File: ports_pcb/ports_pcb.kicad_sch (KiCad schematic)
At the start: 58 parts, among them J1 Conn_01x01_Socket, J10 Conn_01x01_Socket, J100 Joystick, J101 RGB, J102 Printer, J103 Video, J104 Junet, J105 Junet, J106 Tape, J107 5V/2A, J11 Conn_01x01_Socket, J12 Conn_01x01_Socket, J13 Conn_01x01_Socket, J14 Conn_01x01_Socket, J15 Conn_01x01_Socket, J16 Conn_01x01_Socket, J17 Conn_01x01_Socket, J18 Conn_01x01_Socket, J19 Conn_01x01_Socket, J2 Conn_01x01_Socket, J20 Conn_01x01_Socket, J21 Conn_01x01_Socket, J22 Conn_01x01_Socket, J23 Conn_01x01_Socket, J24 Conn_01x01_Socket, J3 Conn_01x01_Socket, J30 Conn_01x01_Socket, J31 Conn_01x01_Socket, J32 Conn_01x01_Socket, J33 Conn_01x01_Socket, J34 Conn_01x01_Socket, J35 Conn_01x01_Socket, J36 Conn_01x01_Socket, J4 Conn_01x01_Socket, J41 RESET1, J42 RESET2, J43 Conn_01x01_Socket, J44 Conn_01x01_Socket, J45 Conn_01x01_Socket, J46 Conn_01x01_Socket, J47 Conn_01x01_Socket, J48 Conn_01x01_Socket, J49 Conn_01x01_Socket, J5 Conn_01x01_Socket, J50 Conn_01x01_Socket, J51 Conn_01x01_Socket, J52 Conn_01x01_Socket, J53 Conn_01x01_Socket, J6 Conn_01x01_Socket, J7 Conn_01x01_Socket, J8 Conn_01x01_Socket, J9 Conn_01x01_Socket, SW1 Reset, SW2 Power

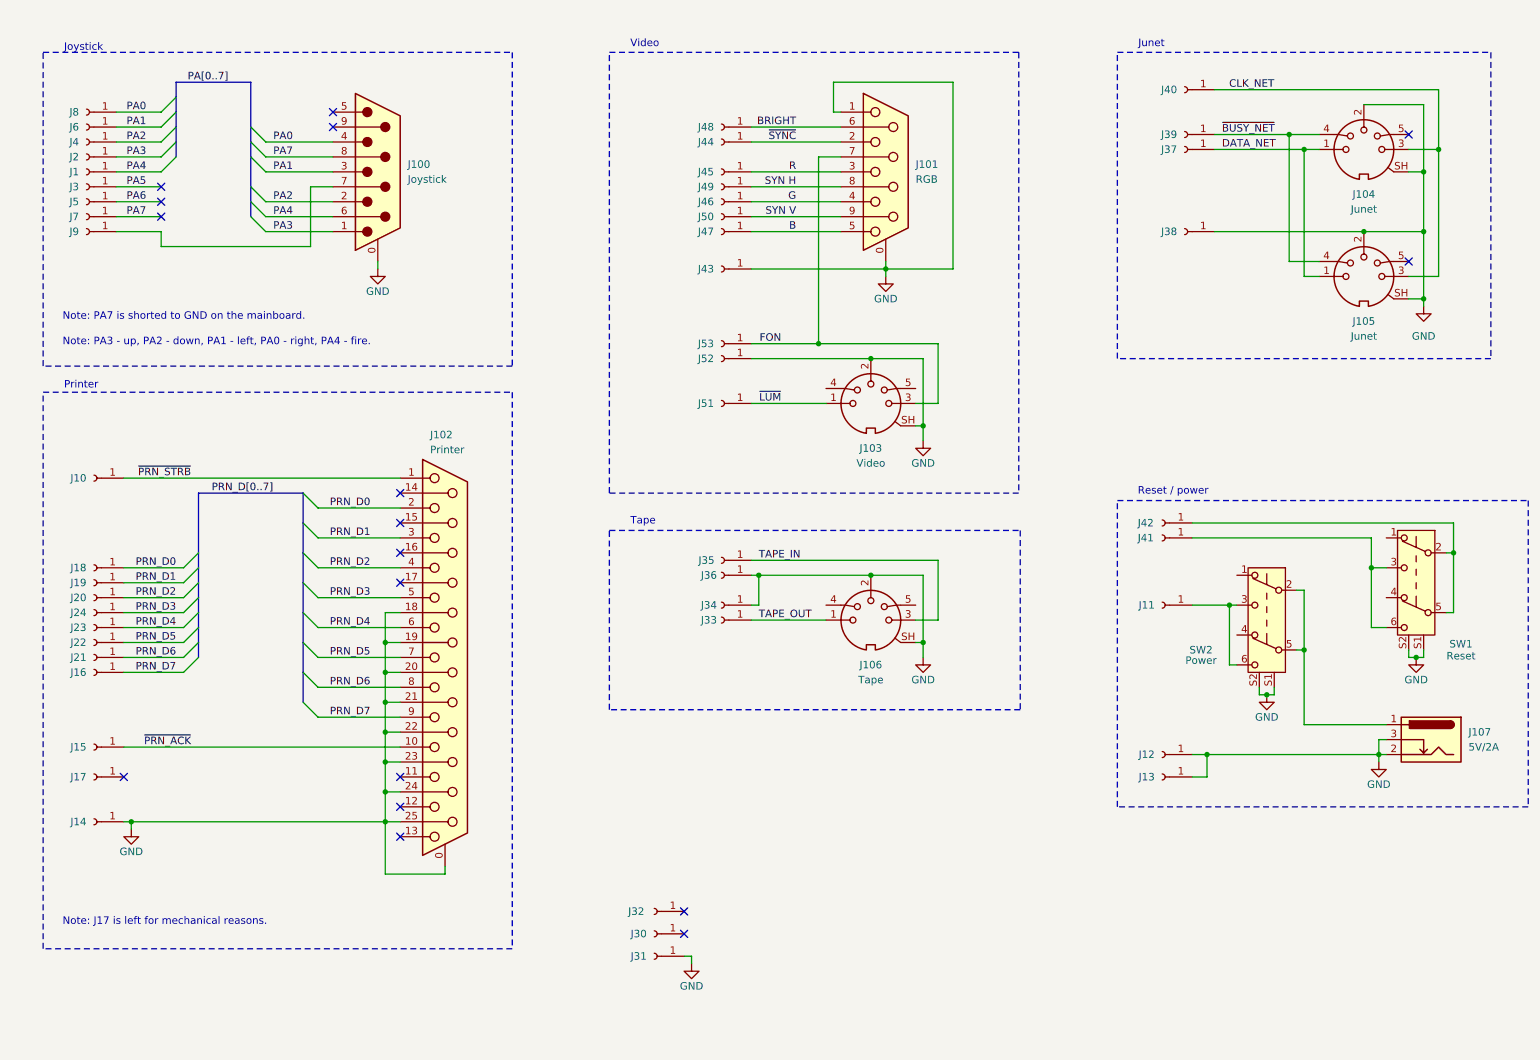
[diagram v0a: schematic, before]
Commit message: ports_pcb: converted to KiCAD 9, fixed 3d models (#1)
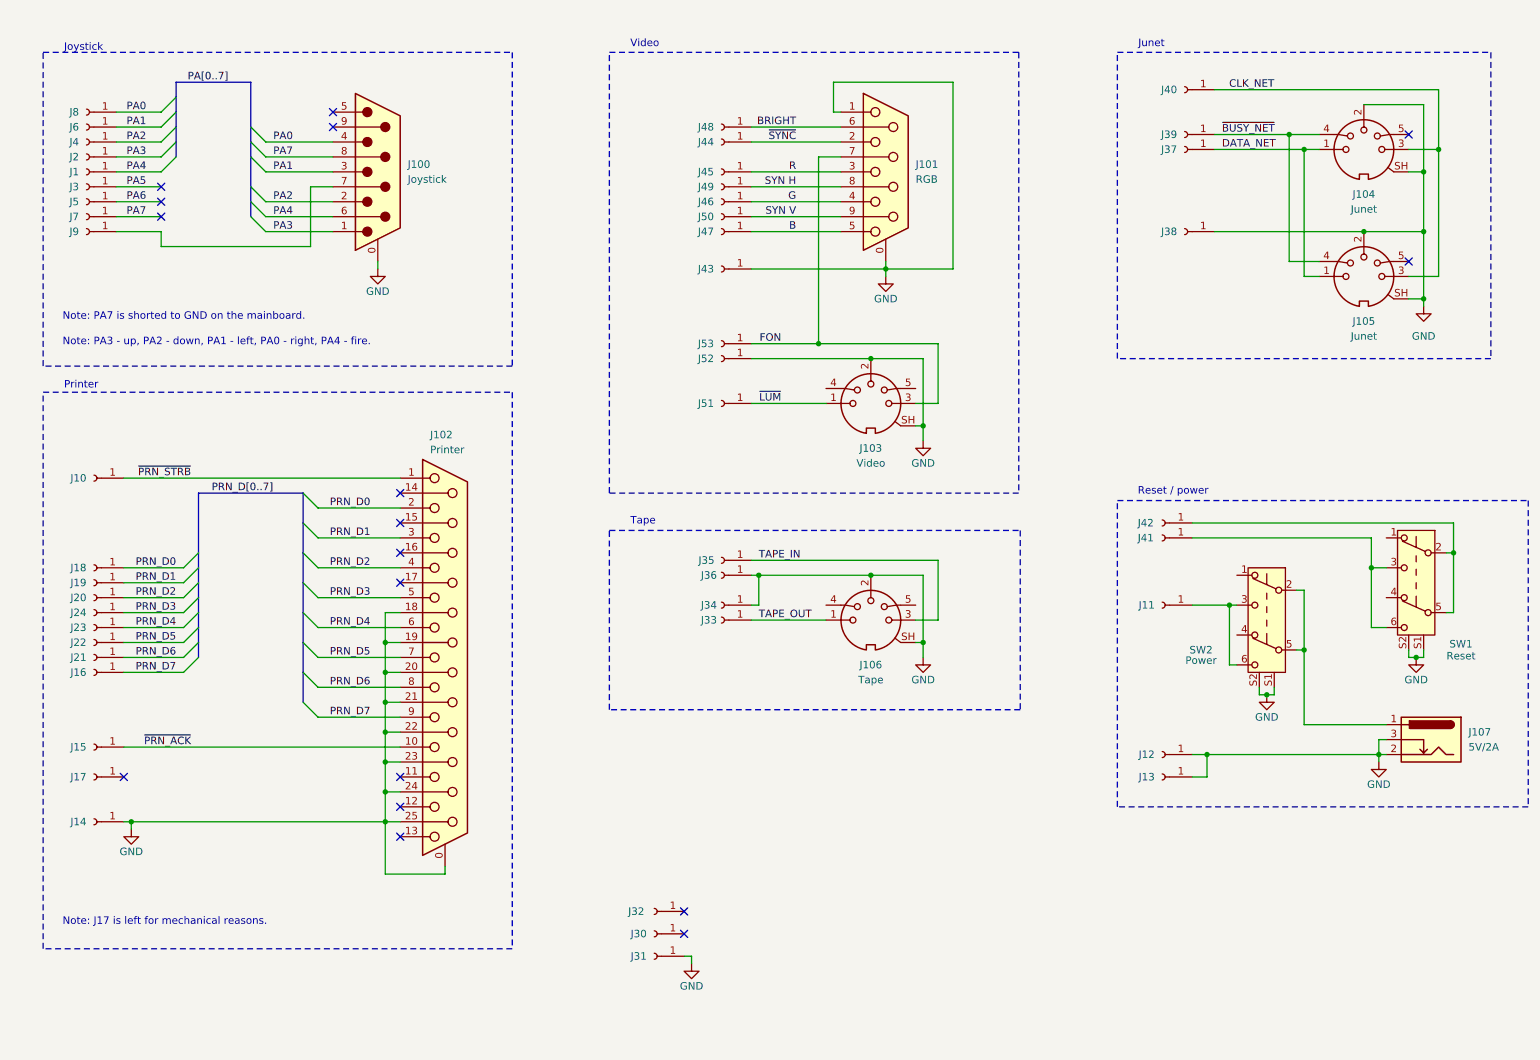
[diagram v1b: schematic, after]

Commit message: Ports PCB: reworked joy (#8) and video (#10)
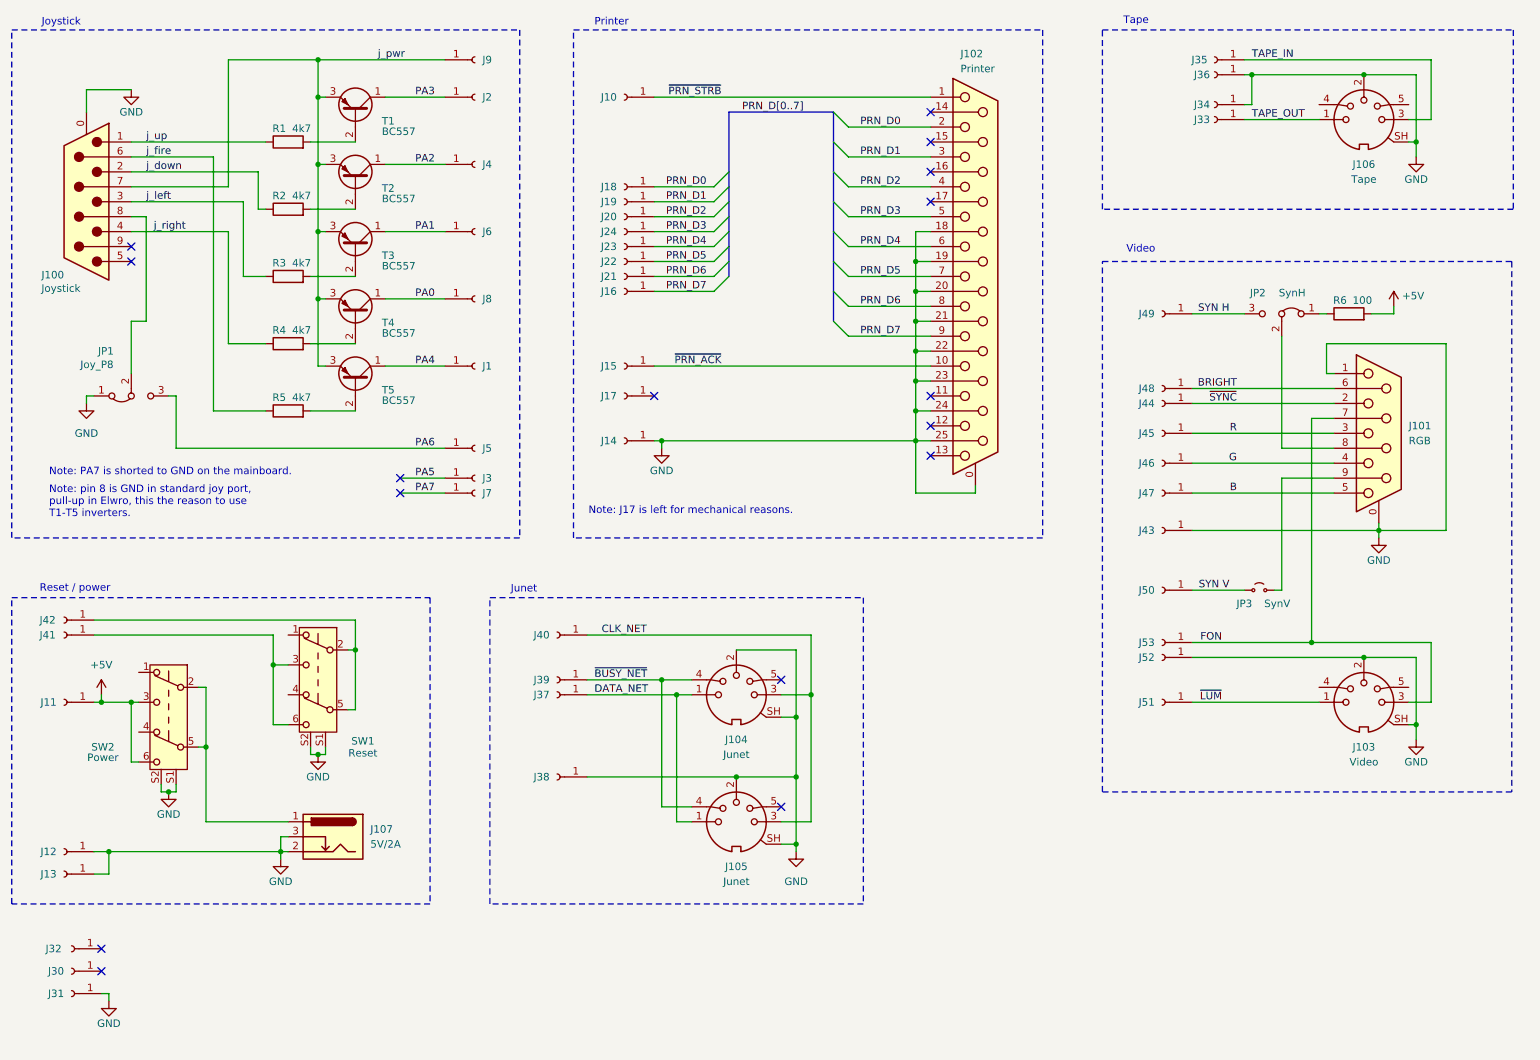
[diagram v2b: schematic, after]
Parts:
- added JP1: Joy_P8, Connector_PinHeader_2.54mm:PinHeader_1x03_P2.54mm_Vertical, symbol Jumper:Jumper_3_Bridged12
- added JP2: SynH, Connector_PinHeader_2.54mm:PinHeader_1x03_P2.54mm_Vertical, symbol Jumper:Jumper_3_Bridged12
- added JP3: SynV, Connector_PinHeader_2.54mm:PinHeader_1x02_P2.54mm_Vertical, symbol Jumper:Jumper_2_Small_Open
- added R1, R2, R3, R4, R5: 4k7, Resistor_THT:R_Axial_DIN0207_L6.3mm_D2.5mm_P10.16mm_Horizontal, symbol Device:R
- added R6: 100, Resistor_THT:R_Axial_DIN0207_L6.3mm_D2.5mm_P10.16mm_Horizontal, symbol Device:R
- added T1, T2, T3, T4, T5: BC557, Package_TO_SOT_THT:TO-92_Inline, symbol Transistor_BJT:BC557
- J100: footprint Connector_Dsub:DSUB-9_Male_Horizontal_P2.77x2.84mm_EdgePinOffset7.70mm_Housed_MountingHolesOffset9.12mm -> Connector_Dsub:DSUB-9_Pins_Horizontal_P2.77x2.84mm_EdgePinOffset7.70mm_Housed_MountingHolesOffset9.12mm
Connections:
- net GND: now also JP1.1 (A)
- net PA0: now also T4.1 (C); no longer J100.4
- net PA1: now also T3.1 (C); no longer J100.3
- net PA2: now also T2.1 (C); no longer J100.2
- net PA3: now also T1.1 (C); no longer J100.1
- net PA4: now also T5.1 (C); no longer J100.6
- net PA6: now also JP1.3 (B)
- net PA7: no longer J100.8
- net SYN H: now also JP2.3 (B); no longer J101.8
- net SYN V: now also JP3.2 (B); no longer J101.9
- net j_pwr: now reaches J100.7, J9.1 (Pin_1)
- net j_pwr: now also T1.3 (E), T2.3 (E), T3.3 (E), T4.3 (E), T5.3 (E)
- net +5V: now reaches J11.1 (Pin_1), SW2.3 (C), SW2.6 (C)
- net +5V: now also R6.2
- new net: JP2.1 (A), R6.1
- new net: R2.2, T2.2 (B)
- new net: R4.2, T4.2 (B)
- new net: J101.8, JP2.2 (C)
- new net: J101.9, JP3.1 (A)
- new net: R3.2, T3.2 (B)
- new net: J100.8, JP1.2 (C)
- new net: R1.2, T1.2 (B)
- new net: R5.2, T5.2 (B)
- new net j_down: J100.2, R2.1
- new net j_fire: J100.6, R5.1
- new net j_left: J100.3, R3.1
- new net j_right: J100.4, R4.1
- new net j_up: J100.1, R1.1
- no-connect marks 17 -> 16
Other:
- note added: "Note: pin 8 is GND in standard joy port, pull-up in Elwro, this the reason to use T1-T5 inverters."
- note removed: "Note: PA3 - up, PA2 - down, PA1 - left, PA0 - right, PA4 - fire."
- moved on the sheet: J1, J10, J101, J102, J103, J104, J105, J106, J107, J11, J12, J13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

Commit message: ports_pcb: added fuse, aux power connector, changed DIN 3d model
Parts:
- added C1: 100nF, Capacitor_THT:C_Disc_D5.0mm_W2.5mm_P2.50mm, symbol Device:C_Small
- added F1: 2A, Fuse:Fuseholder_Clip-5x20mm_Littelfuse_445-030_Inline_P20.50x5.20mm_D1.30mm_Horizontal, symbol Device:Fuse
- added J108: Conn_01x02, Connector_Molex:Molex_KK-254_AE-6410-02A_1x02_P2.54mm_Vertical, symbol Connector_Generic:Conn_01x02
- J101: footprint Connector_Dsub:DSUB-9_Female_Horizontal_P2.77x2.84mm_EdgePinOffset7.70mm_Housed_MountingHolesOffset9.12mm -> Connector_Dsub:DSUB-9_Socket_Horizontal_P2.77x2.84mm_EdgePinOffset7.70mm_Housed_MountingHolesOffset9.12mm
- J102: footprint Connector_Dsub:DSUB-25_Female_Horizontal_P2.77x2.84mm_EdgePinOffset7.70mm_Housed_MountingHolesOffset9.12mm -> Connector_Dsub:DSUB-25_Socket_Horizontal_P2.77x2.84mm_EdgePinOffset7.70mm_Housed_MountingHolesOffset9.12mm
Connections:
- net +5V: now also J108.1 (Pin_1)
- net GND: now also C1.2, J108.2 (Pin_2)
- net at JP2.1 (A), R6.1: now also C1.1
- net at SW2.2 (B), SW2.5 (B): now also F1.1; no longer J107.1
- new net: F1.2, J107.1
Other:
- note added: "Note: pin 8 is GND in a standard joystick port, pull-up in Elwro, this is the reason for using T1-T5 inverters."
- note removed: "Note: pin 8 is GND in standard joy port, pull-up in Elwro, this the reason to use T1-T5 inverters."
- company: (none) -> Przemysław Węgrzyn <pwegrzyn@codepainters.com>
- title: (none) -> Elwro 800 Junio ports breakout board
- moved on the sheet: J101, J103, J43, J44, J45, J46, J47, J48, J49, J50, J51, J52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

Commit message: ports_pcb: fixed a typo in schematic title
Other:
- title: Elwro 800 Junio ports breakout board -> Elwro 800 Junior ports breakout board
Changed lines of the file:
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@@
 	(paper "A4")
 	(title_block
-		(title "Elwro 800 Junio ports breakout board")
+		(title "Elwro 800 Junior ports breakout board")
 		(rev "1.1")
 		(company "Przemysław Węgrzyn <pwegrzyn@codepainters.com>")

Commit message: ports_pcb: excluded Jx headers from BOM
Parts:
- J1, J10, J11, J12, J13, J14, J15, J16, J17, J18, J19, J2, J20, J21, J22, J23, J24, J3, J30, J31, J32, J33, J34, J35, J36, J37, J38, J39, J4, J40, J41, J42, J43, J44, J45, J46, J47, J48, J49, J5, J50, J51, J52, J53, J6, J7, J8, J9: now left out of the parts list
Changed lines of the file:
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@@
 		(unit 1)
 		(exclude_from_sim no)
-		(in_bom yes)
+		(in_bom no)
 		(on_board yes)
 		(dnp no)
@@
 		(unit 1)
 		(exclude_from_sim no)
-		(in_bom yes)
+		(in_bom no)
 		(on_board yes)
 		(dnp no)
@@
 		(unit 1)
 		(exclude_from_sim no)
-		(in_bom yes)
+		(in_bom no)
 		(on_board yes)
 		(dnp no)
@@
 		(unit 1)
 		(exclude_from_sim no)
-		(in_bom yes)
+		(in_bom no)
 		(on_board yes)
 		(dnp no)
@@
 		(unit 1)
 		(exclude_from_sim no)
-		(in_bom yes)
+		(in_bom no)
 		(on_board yes)
 		(dnp no)
@@
 		(unit 1)
 		(exclude_from_sim no)
-		(in_bom yes)
+		(in_bom no)
 		(on_board yes)
 		(dnp no)
@@
 		(unit 1)
 		(exclude_from_sim no)
-		(in_bom yes)
+		(in_bom no)
 		(on_board yes)
 		(dnp no)
@@
 		(unit 1)
 		(exclude_from_sim no)
-		(in_bom yes)
+		(in_bom no)
 		(on_board yes)
 		(dnp no)
@@
 		(unit 1)
 		(exclude_from_sim no)
-		(in_bom yes)
+		(in_bom no)
 		(on_board yes)
 		(dnp no)
@@
 		(unit 1)
 		(exclude_from_sim no)
-		(in_bom yes)
+		(in_bom no)
 		(on_board yes)
 		(dnp no)
@@
 		(unit 1)
 		(exclude_from_sim no)
-		(in_bom yes)
+		(in_bom no)
 		(on_board yes)
 		(dnp no)
@@
 		(unit 1)
 		(exclude_from_sim no)
-		(in_bom yes)
+		(in_bom no)
 		(on_board yes)
 		(dnp no)
@@
 		(unit 1)
 		(exclude_from_sim no)
-		(in_bom yes)
+		(in_bom no)
 		(on_board yes)
 		(dnp no)
@@
 		(unit 1)
 		(exclude_from_sim no)
-		(in_bom yes)
+		(in_bom no)
 		(on_board yes)
 		(dnp no)
@@
 		(unit 1)
 		(exclude_from_sim no)
-		(in_bom yes)
+		(in_bom no)
 		(on_board yes)
 		(dnp no)
@@
 		(unit 1)
 		(exclude_from_sim no)
-		(in_bom yes)
+		(in_bom no)
 		(on_board yes)
 		(dnp no)
@@
 		(unit 1)
 		(exclude_from_sim no)
-		(in_bom yes)
+		(in_bom no)
 		(on_board yes)
 		(dnp no)
@@
 		(unit 1)
 		(exclude_from_sim no)
-		(in_bom yes)
+		(in_bom no)
 		(on_board yes)
 		(dnp no)
@@
 		(unit 1)
 		(exclude_from_sim no)
-		(in_bom yes)
+		(in_bom no)
 		(on_board yes)
 		(dnp no)
@@
 		(unit 1)
 		(exclude_from_sim no)
-		(in_bom yes)
+		(in_bom no)
 		(on_board yes)
 		(dnp no)
@@
 		(unit 1)
 		(exclude_from_sim no)
-		(in_bom yes)
+		(in_bom no)
 		(on_board yes)
 		(dnp no)
@@
 		(unit 1)
 		(exclude_from_sim no)
-		(in_bom yes)
+		(in_bom no)
 		(on_board yes)
 		(dnp no)
@@
 		(unit 1)
 		(exclude_from_sim no)
-		(in_bom yes)
+		(in_bom no)
 		(on_board yes)
 		(dnp no)
@@
 		(unit 1)
 		(exclude_from_sim no)
-		(in_bom yes)
+		(in_bom no)
 		(on_board yes)
 		(dnp no)
@@
 		(unit 1)
 		(exclude_from_sim no)
-		(in_bom yes)
+		(in_bom no)
 		(on_board yes)
 		(dnp no)
@@
 		(unit 1)
 		(exclude_from_sim no)
-		(in_bom yes)
+		(in_bom no)
 		(on_board yes)
 		(dnp no)
@@
 		(unit 1)
 		(exclude_from_sim no)
-		(in_bom yes)
+		(in_bom no)
 		(on_board yes)
 		(dnp no)
@@
 		(unit 1)
 		(exclude_from_sim no)
-		(in_bom yes)
+		(in_bom no)
 		(on_board yes)
 		(dnp no)
@@
 		(unit 1)
 		(exclude_from_sim no)
-		(in_bom yes)
+		(in_bom no)
 		(on_board yes)
 		(dnp no)
@@
 		(unit 1)
 		(exclude_from_sim no)
-		(in_bom yes)
+		(in_bom no)
 		(on_board yes)
 		(dnp no)
@@
 		(unit 1)
 		(exclude_from_sim no)
-		(in_bom yes)
+		(in_bom no)
 		(on_board yes)
 		(dnp no)
@@
 		(unit 1)
 		(exclude_from_sim no)
-		(in_bom yes)
+		(in_bom no)
 		(on_board yes)
 		(dnp no)
@@
 		(unit 1)
 		(exclude_from_sim no)
-		(in_bom yes)
+		(in_bom no)
 		(on_board yes)
 		(dnp no)
@@
 		(unit 1)
 		(exclude_from_sim no)
-		(in_bom yes)
+		(in_bom no)
 		(on_board yes)
 		(dnp no)
@@
 		(unit 1)
 		(exclude_from_sim no)
-		(in_bom yes)
+		(in_bom no)
 		(on_board yes)
 		(dnp no)
@@
 		(unit 1)
 		(exclude_from_sim no)
-		(in_bom yes)
+		(in_bom no)
 		(on_board yes)
 		(dnp no)
@@
 		(unit 1)
 		(exclude_from_sim no)
-		(in_bom yes)
+		(in_bom no)
 		(on_board yes)
 		(dnp no)
@@
 		(unit 1)
 		(exclude_from_sim no)
-		(in_bom yes)
+		(in_bom no)
 		(on_board yes)
 		(dnp no)
@@
 		(unit 1)
 		(exclude_from_sim no)
-		(in_bom yes)
+		(in_bom no)
 		(on_board yes)
 		(dnp no)
@@
 		(unit 1)
 		(exclude_from_sim no)
-		(in_bom yes)
+		(in_bom no)
 		(on_board yes)
 		(dnp no)
@@
 		(unit 1)
 		(exclude_from_sim no)
-		(in_bom yes)
+		(in_bom no)
 		(on_board yes)
 		(dnp no)
@@
 		(unit 1)
 		(exclude_from_sim no)
-		(in_bom yes)
+		(in_bom no)
 		(on_board yes)
 		(dnp no)
@@
 		(unit 1)
 		(exclude_from_sim no)
-		(in_bom yes)
+		(in_bom no)
 		(on_board yes)
 		(dnp no)
@@
 		(unit 1)
 		(exclude_from_sim no)
-		(in_bom yes)
+		(in_bom no)
 		(on_board yes)
 		(dnp no)
@@
 		(unit 1)
 		(exclude_from_sim no)
-		(in_bom yes)
+		(in_bom no)
 		(on_board yes)
 		(dnp no)
@@
 		(unit 1)
 		(exclude_from_sim no)
-		(in_bom yes)
+		(in_bom no)
 		(on_board yes)
 		(dnp no)
@@
 		(unit 1)
 		(exclude_from_sim no)
-		(in_bom yes)
+		(in_bom no)
 		(on_board yes)
 		(dnp no)
@@
 		(unit 1)
 		(exclude_from_sim no)
-		(in_bom yes)
+		(in_bom no)
 		(on_board yes)
 		(dnp no)
